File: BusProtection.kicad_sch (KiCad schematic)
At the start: 90 parts, among them Q1 NX3008NBKS, Q10 MBT2222ADW1T1, Q11 NX3008NBKS, Q12 MBT2222ADW1T1, Q13 NX3008NBKS, Q14 MBT2222ADW1T1, Q15 NX3008NBKS, Q16 MBT2222ADW1T1, Q17 MMBT2907, Q18 MMBT2907, Q19 MMBT2907, Q2 MBT2222ADW1T1, Q3 NX3008NBKS, Q4 MBT2222ADW1T1, Q5 NX3008NBKS, Q6 MBT2222ADW1T1, Q7 NX3008NBKS, Q8 MBT2222ADW1T1, Q9 NX3008NBKS

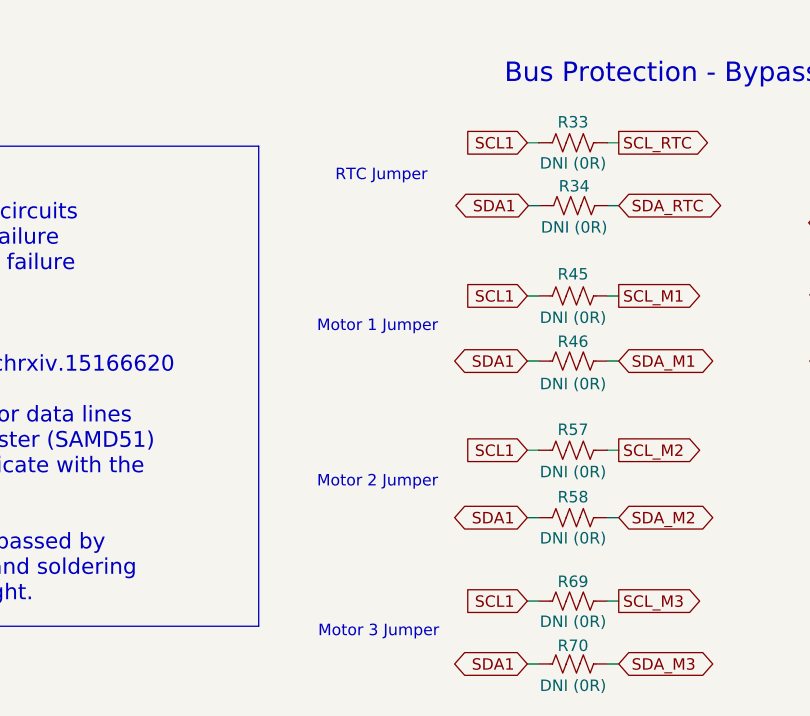
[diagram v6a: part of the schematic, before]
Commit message: Moved Neopixel to be visible through X board hole
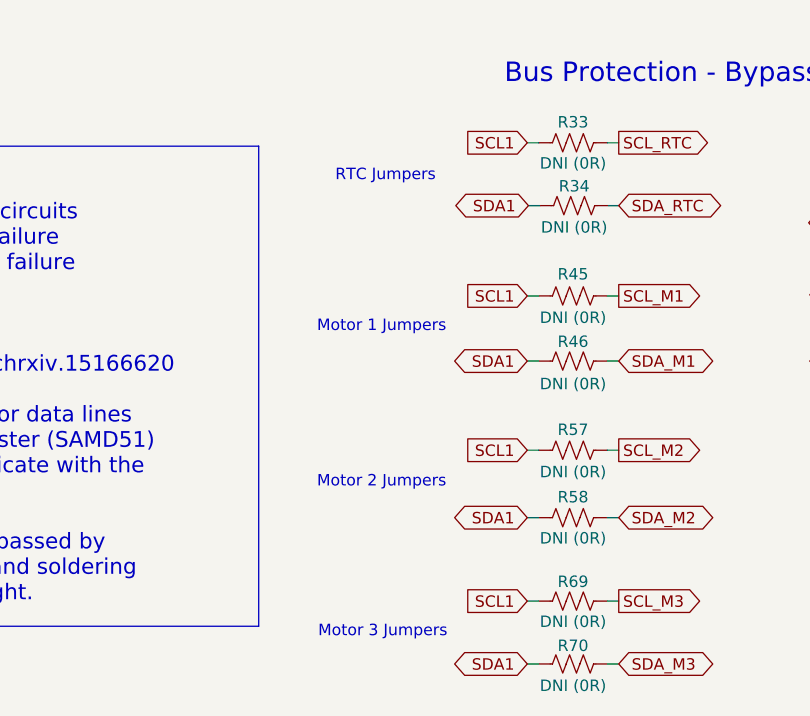
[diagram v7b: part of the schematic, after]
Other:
- note added: "Motor 1 Jumpers"
- note added: "Motor 2 Jumpers"
- note added: "Motor 3 Jumpers"
- note added: "RTC Jumpers"
- note removed: "Motor 1 Jumper"
- note removed: "Motor 2 Jumper"
- note removed: "Motor 3 Jumper"
- note removed: "RTC Jumper"
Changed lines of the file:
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@@
     (rev "B3/01")
     (company "RExLab Carnegie Mellon University")
-    (comment 1 "Z. Manchester")
-    (comment 2 "N. Khera")
-    (comment 3 "M. Holliday")
+    (comment 1 "Z.Manchester")
+    (comment 2 "N.Khera")
+    (comment 3 "M.Holliday")
   )
   (junction (at 240.411 163.449) (diameter 0) (color 0 0 0 0)
@@
     (effects (font (size 2.159 2.159)) (justify left bottom))
   )
-  (text "Motor 3 Jumper" (at 159.639 250.825 0)
+  (text "Motor 3 Jumpers" (at 159.639 250.825 0)
     (effects (font (size 1.27 1.27)) (justify left bottom))
   )
@@
     (effects (font (size 2.159 2.159)) (justify left bottom))
   )
-  (text "Motor 1 Jumper" (at 159.512 216.916 0)
+  (text "Motor 1 Jumpers" (at 159.512 216.916 0)
     (effects (font (size 1.27 1.27)) (justify left bottom))
   )
@@
     (effects (font (size 2.159 2.159)) (justify left bottom))
   )
-  (text "RTC Jumper" (at 161.544 200.152 0)
+  (text "RTC Jumpers" (at 161.544 200.152 0)
     (effects (font (size 1.27 1.27)) (justify left bottom))
   )
@@
     (effects (font (size 1.27 1.27)) (justify left bottom))
   )
-  (text "Motor 2 Jumper" (at 159.512 234.188 0)
+  (text "Motor 2 Jumpers" (at 159.512 234.188 0)
     (effects (font (size 1.27 1.27)) (justify left bottom))
   )
